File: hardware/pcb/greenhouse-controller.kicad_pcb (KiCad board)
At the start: 2 copper layers, 208 x 132 mm, 71 parts, among them J1 Motor 2, J10 ALARM contact, J11 AC-Mains, J12 DM1AA-SF-PEJ72, J2 24V in, J3 I2C Display, J4 Keypad, J5 MODBUS RS485 S200, J6 Motor 3, J7 Motor 1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

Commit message: Revision of PCB.
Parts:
- added G***: LOGO_LogoRFSee_28x5-6mm, my-KiCad-library:LOGO_LogoRFSee_28x5-6mm, F.Cu at (72.4, 45.7)
- moved C3 17.9 mm to (154.9, 47.0), turned to -90 degrees
- moved C1 11.4 mm to (182.9, 121.3), turned to -90 degrees
- moved U3 6.84 mm to (179.1, 115.6), turned to -90 degrees
- moved J4 1.27 mm to (177.8, 106.7)
- moved U1 1.17 mm to (163.0, 68.6)
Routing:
- net /OPTO_INPUT: track 8.87 -> 213.4 mm
- net /3V3: track 0.00 -> 162.3 mm, vias 0 -> 2
- net /RELAY_M1_CLOSE: track 6.31 -> 156.9 mm, vias 0 -> 1
- net /RELAY_M2_OPEN: track 5.34 -> 110.6 mm, vias 0 -> 2
- net /SD_CS: track 0.00 -> 105.1 mm
- net /RELAY_M1_OPEN: track 5.31 -> 106.4 mm
- net /RELAY_M3_CLOSE: track 6.31 -> 103.1 mm
- net /SD_CLK: track 0.00 -> 95.2 mm
- net /GND: track 468.8 -> 560.4 mm, vias 164 -> 291
- net /SD_MOSI: track 0.00 -> 91.5 mm
- net Net-(BT1-+): track 0.00 -> 90.4 mm
- net /SD_MISO: track 0.00 -> 87.4 mm
- net /RELAY_M3_OPEN: track 5.31 -> 89.9 mm
- net /5V: track 311.9 -> 393.8 mm, vias 4 -> 6
- net /KP_ROW1: track 0.00 -> 80.1 mm
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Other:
- board text added: "Remko Welling (remko@rfsee.nl) 24-4-2026"
- board text removed: "Remko Welling (remko@rfsee.nl) 15-4-2026"

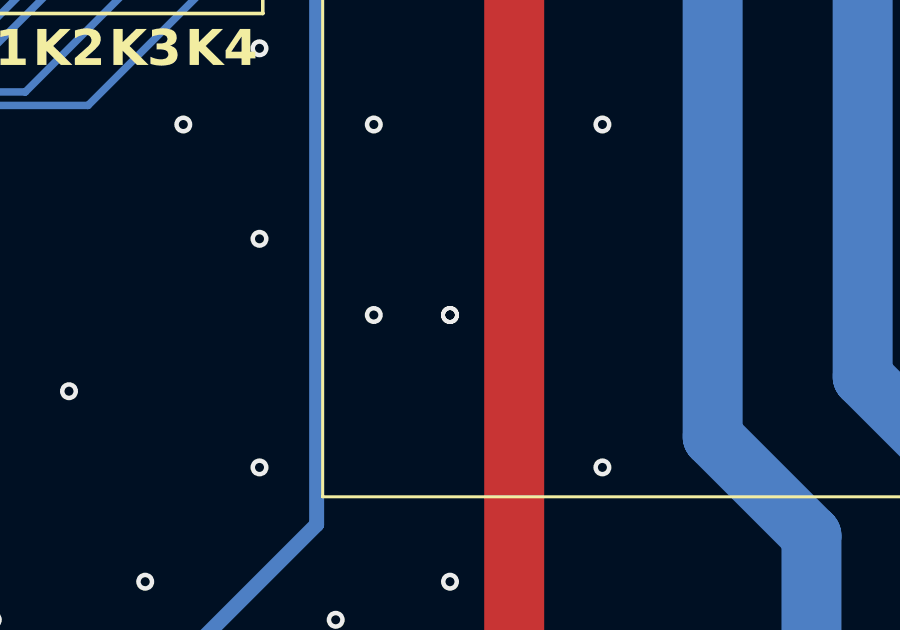
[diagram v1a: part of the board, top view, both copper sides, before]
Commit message: Committed PCB is ordered 1x
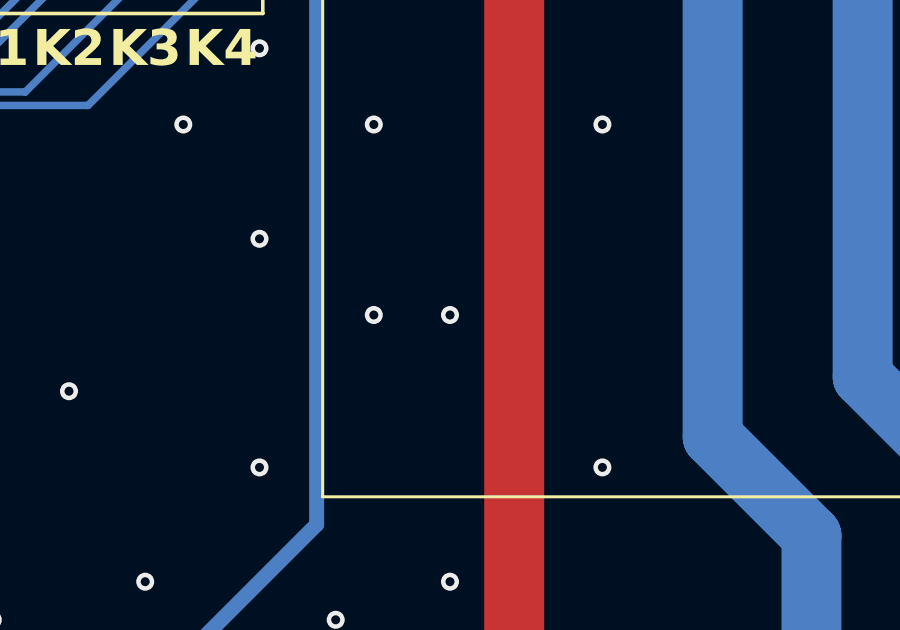
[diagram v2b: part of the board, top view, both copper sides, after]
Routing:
- net /GND: vias 291 -> 290
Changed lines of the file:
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@@
-	)
-	(via
-		(at 203.2 118.11)
-		(size 0.6)
-		(drill 0.3)
-		(layers "F.Cu" "B.Cu")
-		(free yes)
-		(net "/GND")
 	)
 	(via
@@
 	)
 	(segment
+		(start 184.13 25.42)
+		(end 174.41 35.14)
+		(width 1.5)
+		(layer "B.Cu")
+		(net "/GND")
+	)
+	(segment
+		(start 134.955 51.915)
+		(end 125.6575 42.6175)
+		(width 0.5)
+		(layer "B.Cu")
+		(net "/GND")
+	)
+	(segment
+		(start 185.7125 56.8075)
+		(end 186.055 57.15)
+		(width 0.5)
+		(layer "B.Cu")
+		(net "/GND")
+	)
+	(segment
+		(start 186.055 57.15)
+		(end 186.055 63.1575)
+		(width 0.5)
+		(layer "B.Cu")
+		(net "/GND")
+	)
+	(segment
+		(start 65.79 122.17)
+		(end 73.495 114.465)
+		(width 1)
+		(layer "B.Cu")
+		(net "/GND")
+	)
+	(segment
+		(start 125.6575 35.242012)
+		(end 125.6575 42.6175)
+		(width 0.5)
+		(layer "B.Cu")
+		(net "/GND")
+	)
+	(segment
+		(start 194.945 31.75)
+		(end 194.945 26.67)
+		(width 1.5)
+		(layer "B.Cu")
+		(net "/GND")
+	)
+	(segment
 		(start 193.695 25.42)
 		(end 184.13 25.42)
@@
 	)
 	(segment
-		(start 134.955 51.915)
-		(end 125.6575 42.6175)
+		(start 186.055 46.99)
+		(end 189.955 43.09)
+		(width 1.5)
+		(layer "B.Cu")
+		(net "/GND")
+	)
+	(segment
+		(start 125.73 35.169512)
+		(end 125.6575 35.242012)
 		(width 0.5)
 		(layer "B.Cu")
@@
 	)
 	(segment
-		(start 185.7125 56.8075)
-		(end 186.055 57.15)
-		(width 0.5)
-		(layer "B.Cu")
-		(net "/GND")
-	)
-	(segment
-		(start 186.055 57.15)
-		(end 186.055 63.1575)
-		(width 0.5)
+		(start 73.495 114.465)
+		(end 73.495 112.805)
+		(width 1)
+		(layer "B.Cu")
+		(net "/GND")
+	)
+	(segment
+		(start 186.055 50.165)
+		(end 186.055 46.99)
+		(width 1.5)
+		(layer "B.Cu")
+		(net "/GND")
+	)
+	(segment
+		(start 189.955 38.63)
+		(end 189.955 36.74)
+		(width 1.5)
+		(layer "B.Cu")
+		(net "/GND")
+	)
+	(segment
+		(start 194.945 26.67)
+		(end 193.695 25.42)
+		(width 1.5)
 		(layer "B.Cu")
 		(net "/GND")
@@
 	)
 	(segment
-		(start 65.79 122.17)
-		(end 73.495 114.465)
-		(width 1)
-		(layer "B.Cu")
-		(net "/GND")
-	)
-	(segment
-		(start 125.6575 35.242012)
-		(end 125.6575 42.6175)
-		(width 0.5)
-		(layer "B.Cu")
-		(net "/GND")
-	)
-	(segment
-		(start 186.055 46.99)
-		(end 189.955 43.09)
-		(width 1.5)
-		(layer "B.Cu")
-		(net "/GND")
-	)
-	(segment
-		(start 194.945 31.75)
-		(end 194.945 26.67)
-		(width 1.5)
-		(layer "B.Cu")
-		(net "/GND")
-	)
-	(segment
-		(start 125.73 35.169512)
-		(end 125.6575 35.242012)
-		(width 0.5)
-		(layer "B.Cu")
-		(net "/GND")
-	)
-	(segment
-		(start 73.495 114.465)
-		(end 73.495 112.805)
-		(width 1)
-		(layer "B.Cu")
-		(net "/GND")
-	)
-	(segment
-		(start 186.055 50.165)
-		(end 186.055 46.99)
-		(width 1.5)
-		(layer "B.Cu")
-		(net "/GND")
-	)
-	(segment
-		(start 184.13 25.42)
-		(end 174.41 35.14)
-		(width 1.5)
-		(layer "B.Cu")
-		(net "/GND")
-	)
-	(segment
 		(start 189.955 43.09)
 		(end 189.955 41.17)
@@
 	)
 	(segment
-		(start 194.945 26.67)
-		(end 193.695 25.42)
-		(width 1.5)
-		(layer "B.Cu")
-		(net "/GND")
-	)
-	(segment
 		(start 151.51 92.71)
 		(end 155.956 92.71)
@@
 		(layer "B.Cu")
 		(net "/GND")
-	)
-	(segment
-		(start 189.955 38.63)
-		(end 189.955 36.74)
-		(width 1.5)
-		(layer "B.Cu")
-		(net "/GND")

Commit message: Updated PCB design to version 1.0.0
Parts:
- D14: value LED Amber -> Green
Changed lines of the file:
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@@
 	(title_block
 		(title "PCB Kas-controller Wenumseveld")
-		(date "2026-04-15")
+		(date "2026-04-24")
 		(rev "Remko Welling")
 		(company "RFSee")
 		(comment 1 "remko@rfsee.nl")
 		(comment 2 "https://www.rfsee.nl")
+		(comment 3 "V 1.0.0")
 	)
 	(layers
@@
 		)
 		(property "Value" "SIT65HVD08P"
-			(at 3.81 9.95 90)
+			(at -2.54 3.81 180)
 			(layer "F.Fab")
 			(effects
@@
 			)
 		)
-		(property "Value" "LED Amber"
-			(at 0 1.65 0)
+		(property "Value" "Green"
+			(at 0.635 1.65 0)
 			(layer "F.Fab")
 			(effects
@@
 		)
 		(property "Value" "Keypad"
-			(at 0 20.16 90)
+			(at 0 22.86 180)
 			(layer "F.Fab")
 			(effects
@@
 		)
 		(property "Value" "120"
-			(at 0 1.83 0)
+			(at -4.165 0 0)
 			(layer "F.Fab")
 			(effects
@@
 		)
 		(property "Value" "20K"
-			(at 0 1.83 90)
+			(at 2.54 0 180)
 			(layer "F.Fab")
 			(effects
@@
 		)
 		(property "Value" "AC-Mains"
-			(at 5 5.72 0)
+			(at 5 9.271 0)
 			(layer "F.Fab")
 			(effects
@@
 		)
 		(fp_text user "${REFERENCE}"
-			(at 5 3.2 0)
+			(at -0.619143 6.731 0)
 			(layer "F.Fab")
 			(effects
@@
 		)
 		(property "Value" "20K"
-			(at 0 1.83 90)
+			(at -2.54 0 180)
 			(layer "F.Fab")
 			(effects
@@
 		)
 		(property "Value" "Load enable"
-			(at -2.54 4.419 180)
+			(at -2.54 0.355 0)
 			(layer "F.Fab")
 			(effects
@@
 		)
 		(property "Value" "MODBUS RS485 FG6485A"
-			(at 7.5 5.72 0)
+			(at 7.5 9.271 0)
 			(layer "F.Fab")
 			(effects
@@
 		)
 		(fp_text user "${REFERENCE}"
-			(at 7.5 3.2 0)
+			(at -0.650857 6.731 0)
 			(layer "F.Fab")
 			(effects
@@
 		)
 		(property "Value" "Motor 1"
-			(at 7.5 5.72 0)
+			(at 7.5 9.271 0)
 			(layer "F.Fab")
 			(effects
@@
 		)
 		(fp_text user "${REFERENCE}"
-			(at 7.5 3.2 0)
+			(at -0.853429 6.731 0)
 			(layer "F.Fab")
 			(effects
@@
 		)
 		(property "Value" "Motor 2"
-			(at 7.5 5.72 0)
+			(at 7.5 9.271 0)
 			(layer "F.Fab")
 			(effects
@@
 		)
 		(fp_text user "${REFERENCE}"
-			(at 7.5 3.2 0)
+			(at -0.362572 6.731 0)
 			(layer "F.Fab")
 			(effects
@@
 		)
 		(property "Value" "ALARM contact"
-			(at 2.5 5.72 0)
+			(at 2.625714 9.271 0)
 			(layer "F.Fab")
 			(effects
@@
 		)
 		(fp_text user "${REFERENCE}"
-			(at 2.5 3.2 0)
+			(at -1.184286 6.731 0)
 			(layer "F.Fab")
 			(effects
@@
 		)
 		(property "Value" "Motor 3"
-			(at 7.5 5.72 0)
+			(at 7.5 9.271 0)
 			(layer "F.Fab")
 			(effects
@@
 		)
 		(fp_text user "${REFERENCE}"
-			(at 7.5 3.2 0)
+			(at 0.128285 6.731 0)
 			(layer "F.Fab")
 			(effects
@@
 		)
 		(property "Value" "MODBUS RS485 S200"
-			(at 17.5 5.72 0)
+			(at 17.5 9.271 0)
 			(layer "F.Fab")
 			(effects
@@
 		)
 		(fp_text user "${REFERENCE}"
-			(at 17.5 3.2 0)
+			(at -1.43 6.731 0)
 			(layer "F.Fab")
 			(effects
@@
 		)
 		(property "Value" "100n"
-			(at 0 -1.905 90)
+			(at 3.175 0 0)
 			(layer "F.Fab")
 			(effects
@@
 		)
 		(property "Value" "24V in"
-			(at 2.5 5.72 0)
+			(at 2.5 9.271 0)
 			(layer "F.Fab")
 			(effects
@@
 		)
 		(fp_text user "${REFERENCE}"
-			(at 2.5 3.2 0)
+			(at -1.478286 6.731 0)
 			(layer "F.Fab")
 			(effects

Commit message: PCB bump to V1.1.0
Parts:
- removed J5: MODBUS RS485 S200, TerminalBlock_Phoenix:TerminalBlock_Phoenix_MKDS-1,5-8_1x08_P5.00mm_Horizontal
- added J13: MODBUS RS485 S200, TerminalBlock_Phoenix:TerminalBlock_Phoenix_MKDS-1,5-4_1x04_P5.00mm_Horizontal, F.Cu at (170.2, 134.1)
- D14: value Green -> LED Amber
- moved G*** 65.6 mm to (58.9, -13.7)
- moved G*** 9.92 mm to (62.5, 46.2)
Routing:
- net /RS485-B: track 73.1 -> 57.6 mm
- net /RS485-A: track 64.5 -> 76.2 mm
- net /24V: track 221.5 -> 227.4 mm
- net /GND: track 560.4 -> 562.0 mm, vias 290 -> 293
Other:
- board text added: "KAS-Controller V1.1.0"
- board text added: "Remko Welling (remko@rfsee.nl) 1-5-2026"
- board text removed: "KAS-Controller"
- board text removed: "Remko Welling (remko@rfsee.nl) 24-4-2026"
